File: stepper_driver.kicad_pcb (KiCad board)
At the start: 2 copper layers, 41.9 x 41.9 mm, 13 parts, among them T1 TERM_BLK_4_PIN_0.1_PITCH, T2 TERM_BLK_ANG_2_PIN_3.5MM_PITCH, T3 TERM_BLK_2_PIN_0.1_PITCH, T4 TERM_BLK_2_PIN_0.1_PITCH

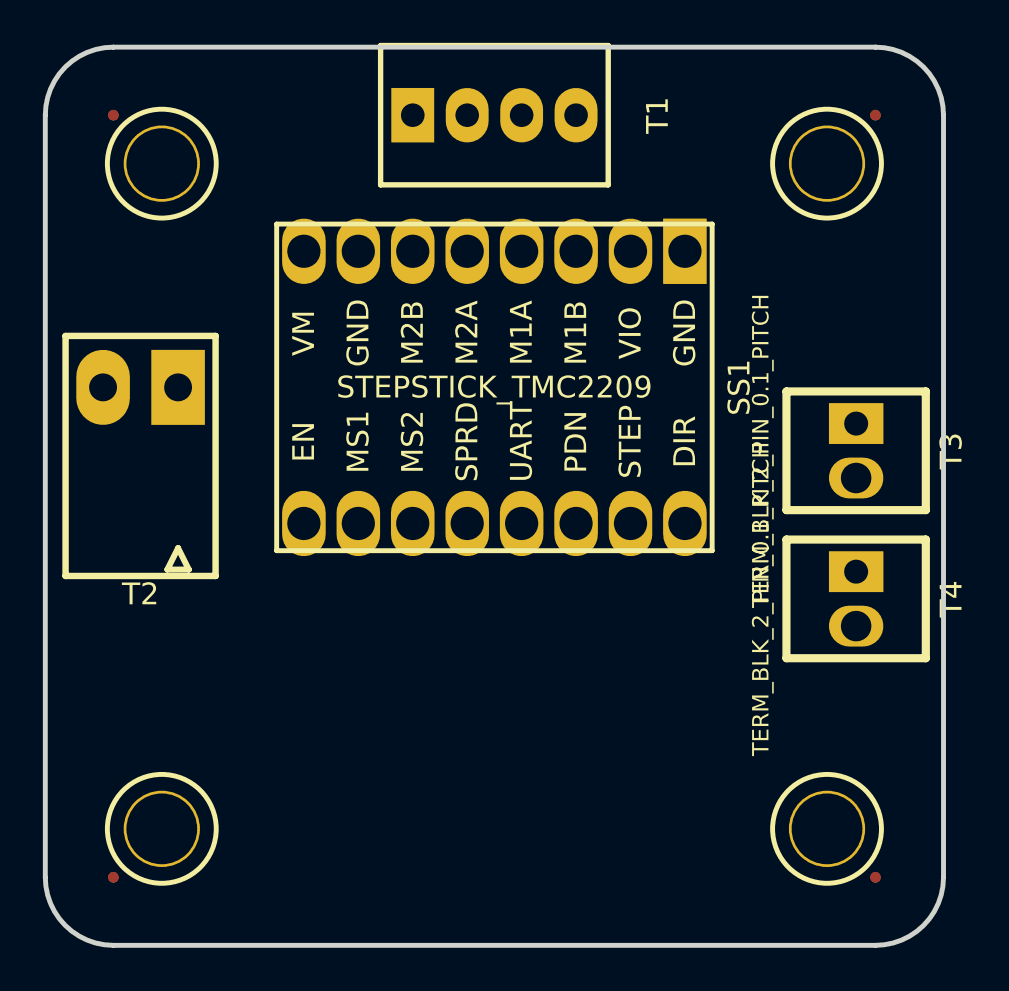
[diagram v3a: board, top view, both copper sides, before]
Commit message: Add power components
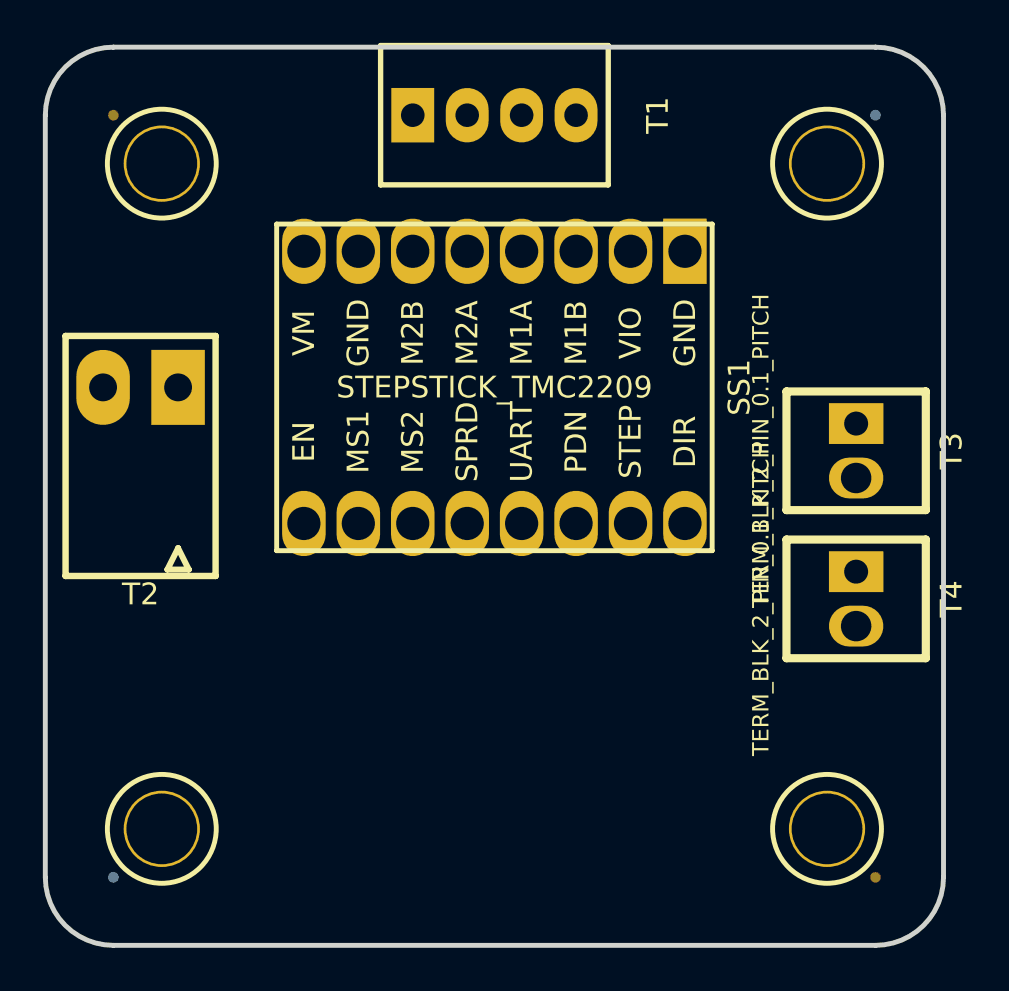
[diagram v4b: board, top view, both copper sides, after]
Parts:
- FID2, FID4: moved to B.Cu
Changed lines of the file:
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@@
       (effects (font (size 0.254 0.254) (thickness 0.0635)))
     )
+    (fp_circle (center 0 0) (end 0.5 0) (layer F.Fab) (width 0.1))
     (fp_circle (center 0 0) (end 0.75 0) (layer F.CrtYd) (width 0.05))
-    (fp_circle (center 0 0) (end 0.5 0) (layer F.Fab) (width 0.1))
     (fp_text user %R (at 0 0) (layer F.Fab)
       (effects (font (size 0.2 0.2) (thickness 0.04)))
@@
       (solder_mask_margin 0.25) (clearance 0.25))
   )
-  (module stepper_driver:FIDUCIAL (layer F.Cu)
+  (module stepper_driver:FIDUCIAL (layer B.Cu)
     (at 157.48 71.12)
     (descr "Circular Fiducial, 0.5mm bare copper top; 1mm keepout (Level C)")
     (tags marker)
     (attr virtual)
-    (fp_text reference FID2 (at 0 -1.016) (layer F.Fab)
-      (effects (font (size 0.254 0.254) (thickness 0.0635)))
-    )
-    (fp_text value FIDUCIAL (at 0 1.016) (layer F.Fab)
-      (effects (font (size 0.254 0.254) (thickness 0.0635)))
-    )
-    (fp_circle (center 0 0) (end 0.5 0) (layer F.Fab) (width 0.1))
-    (fp_circle (center 0 0) (end 0.75 0) (layer F.CrtYd) (width 0.05))
-    (fp_text user %R (at 0 0) (layer F.Fab)
-      (effects (font (size 0.2 0.2) (thickness 0.04)))
-    )
-    (pad ~ smd circle (at 0 0) (size 0.5 0.5) (layers F.Cu F.Mask)
+    (fp_text reference FID2 (at 0 1.016) (layer B.Fab)
+      (effects (font (size 0.254 0.254) (thickness 0.0635)) (justify mirror))
+    )
+    (fp_text value FIDUCIAL (at 0 -1.016) (layer B.Fab)
+      (effects (font (size 0.254 0.254) (thickness 0.0635)) (justify mirror))
+    )
+    (fp_circle (center 0 0) (end 0.75 0) (layer B.CrtYd) (width 0.05))
+    (fp_circle (center 0 0) (end 0.5 0) (layer B.Fab) (width 0.1))
+    (fp_text user %R (at 0 0) (layer B.Fab)
+      (effects (font (size 0.2 0.2) (thickness 0.04)) (justify mirror))
+    )
+    (pad ~ smd circle (at 0 0) (size 0.5 0.5) (layers B.Cu B.Mask)
       (solder_mask_margin 0.25) (clearance 0.25))
   )
@@
       (effects (font (size 0.254 0.254) (thickness 0.0635)))
     )
+    (fp_circle (center 0 0) (end 0.5 0) (layer F.Fab) (width 0.1))
     (fp_circle (center 0 0) (end 0.75 0) (layer F.CrtYd) (width 0.05))
-    (fp_circle (center 0 0) (end 0.5 0) (layer F.Fab) (width 0.1))
     (fp_text user %R (at 0 0) (layer F.Fab)
       (effects (font (size 0.2 0.2) (thickness 0.04)))
@@
       (solder_mask_margin 0.25) (clearance 0.25))
   )
-  (module stepper_driver:FIDUCIAL (layer F.Cu)
+  (module stepper_driver:FIDUCIAL (layer B.Cu)
     (at 121.92 106.68)
     (descr "Circular Fiducial, 0.5mm bare copper top; 1mm keepout (Level C)")
     (tags marker)
     (attr virtual)
-    (fp_text reference FID4 (at 0 -1.016) (layer F.Fab)
-      (effects (font (size 0.254 0.254) (thickness 0.0635)))
-    )
-    (fp_text value FIDUCIAL (at 0 1.016) (layer F.Fab)
-      (effects (font (size 0.254 0.254) (thickness 0.0635)))
-    )
-    (fp_circle (center 0 0) (end 0.5 0) (layer F.Fab) (width 0.1))
-    (fp_circle (center 0 0) (end 0.75 0) (layer F.CrtYd) (width 0.05))
-    (fp_text user %R (at 0 0) (layer F.Fab)
-      (effects (font (size 0.2 0.2) (thickness 0.04)))
-    )
-    (pad ~ smd circle (at 0 0) (size 0.5 0.5) (layers F.Cu F.Mask)
+    (fp_text reference FID4 (at 0 1.016) (layer B.Fab)
+      (effects (font (size 0.254 0.254) (thickness 0.0635)) (justify mirror))
+    )
+    (fp_text value FIDUCIAL (at 0 -1.016) (layer B.Fab)
+      (effects (font (size 0.254 0.254) (thickness 0.0635)) (justify mirror))
+    )
+    (fp_circle (center 0 0) (end 0.75 0) (layer B.CrtYd) (width 0.05))
+    (fp_circle (center 0 0) (end 0.5 0) (layer B.Fab) (width 0.1))
+    (fp_text user %R (at 0 0) (layer B.Fab)
+      (effects (font (size 0.2 0.2) (thickness 0.04)) (justify mirror))
+    )
+    (pad ~ smd circle (at 0 0) (size 0.5 0.5) (layers B.Cu B.Mask)
       (solder_mask_margin 0.25) (clearance 0.25))
   )
@@
       (effects (font (size 1.016 1.016) (thickness 0.254)))
     )
+    (fp_line (start 7.62 -10.16) (end -7.62 -10.16) (layer F.SilkS) (width 0.2286))
+    (fp_line (start 7.62 10.16) (end 7.62 -10.16) (layer F.SilkS) (width 0.2286))
+    (fp_line (start -7.62 10.16) (end 7.62 10.16) (layer F.SilkS) (width 0.2286))
     (fp_line (start -7.62 -10.16) (end -7.62 10.16) (layer F.SilkS) (width 0.2286))
-    (fp_line (start -7.62 10.16) (end 7.62 10.16) (layer F.SilkS) (width 0.2286))
-    (fp_line (start 7.62 10.16) (end 7.62 -10.16) (layer F.SilkS) (width 0.2286))
-    (fp_line (start 7.62 -10.16) (end -7.62 -10.16) (layer F.SilkS) (width 0.2286))
     (fp_text user DIR (at 2.54 -8.89 90) (layer F.SilkS)
       (effects (font (size 1.016 1.016) (thickness 0.254)))
@@
       (effects (font (size 0.762 0.762) (thickness 0.1905)))
     )
+    (fp_line (start -5.31 -3.25) (end 5.31 -3.25) (layer F.SilkS) (width 0.25))
+    (fp_line (start 5.31 -3.25) (end 5.31 3.25) (layer F.SilkS) (width 0.25))
+    (fp_line (start -5.31 3.25) (end 5.31 3.25) (layer F.SilkS) (width 0.25))
     (fp_line (start -5.31 -3.25) (end -5.31 3.25) (layer F.SilkS) (width 0.25))
-    (fp_line (start -5.31 3.25) (end 5.31 3.25) (layer F.SilkS) (width 0.25))
-    (fp_line (start 5.31 -3.25) (end 5.31 3.25) (layer F.SilkS) (width 0.25))
-    (fp_line (start -5.31 -3.25) (end 5.31 -3.25) (layer F.SilkS) (width 0.25))
     (pad 1 thru_hole rect (at -3.81 0) (size 2 2.54) (drill 1.1) (layers *.Cu *.Mask)
       (net 5 /B-))
@@
       (effects (font (size 0.508 0.508) (thickness 0.127)))
     )
+    (fp_line (start -3.5 -8.8) (end -3.5 2.4) (layer F.SilkS) (width 0.3))
+    (fp_line (start -3.5 2.4) (end 3.5 2.4) (layer F.SilkS) (width 0.3))
+    (fp_line (start 3.5 -8.8) (end 3.5 2.4) (layer F.SilkS) (width 0.3))
+    (fp_line (start -3.5 -8.8) (end 3.5 -8.8) (layer F.SilkS) (width 0.3))
+    (fp_line (start -2.25 -8.5) (end -1.25 -8.5) (layer F.SilkS) (width 0.2794))
+    (fp_line (start -1.25 -8.5) (end -1.75 -7.5) (layer F.SilkS) (width 0.2794))
     (fp_line (start -1.75 -7.5) (end -2.25 -8.5) (layer F.SilkS) (width 0.2794))
-    (fp_line (start -1.25 -8.5) (end -1.75 -7.5) (layer F.SilkS) (width 0.2794))
-    (fp_line (start -2.25 -8.5) (end -1.25 -8.5) (layer F.SilkS) (width 0.2794))
-    (fp_line (start -3.5 -8.8) (end 3.5 -8.8) (layer F.SilkS) (width 0.3))
-    (fp_line (start 3.5 -8.8) (end 3.5 2.4) (layer F.SilkS) (width 0.3))
-    (fp_line (start -3.5 2.4) (end 3.5 2.4) (layer F.SilkS) (width 0.3))
-    (fp_line (start -3.5 -8.8) (end -3.5 2.4) (layer F.SilkS) (width 0.3))
     (pad 1 thru_hole rect (at -1.75 0 180) (size 2.5 3.5) (drill 1.3) (layers *.Cu *.Mask))
     (pad 2 thru_hole oval (at 1.75 0 180) (size 2.5 3.5) (drill 1.3) (layers *.Cu *.Mask)
@@
     (at 156.578299 86.779101 270)
     (fp_text reference T3 (at 0 -4.445 90) (layer F.SilkS)
+      (effects (font (size 1.016 1.016) (thickness 0.254)))
+    )
+    (fp_text value TERM_BLK_2_PIN_0.1_PITCH (at 0 4.445 270) (layer F.SilkS)
+      (effects (font (size 0.762 0.762) (thickness 0.1905)))
+    )
+    (fp_line (start -2.7686 -3.2512) (end -2.7686 3.2512) (layer F.SilkS) (width 0.381))
+    (fp_line (start -2.7686 3.2512) (end 2.7686 3.2512) (layer F.SilkS) (width 0.381))
+    (fp_line (start 2.7686 -3.2512) (end 2.7686 3.2512) (layer F.SilkS) (width 0.381))
+    (fp_line (start -2.7686 -3.2512) (end 2.7686 -3.2512) (layer F.SilkS) (width 0.381))
+    (pad 1 thru_hole rect (at -1.27 0 270) (size 1.905 2.54) (drill 1.1176) (layers *.Cu *.Mask))
+    (pad 2 thru_hole oval (at 1.27 0 270) (size 1.905 2.54) (drill 1.4224) (layers *.Cu *.Mask))
+  )
+  (module stepper_driver:TERM_BLK_2_PIN_0.1_PITCH (layer F.Cu)
+    (at 156.578299 93.689101 270)
+    (fp_text reference T4 (at 0 -4.445 90) (layer F.SilkS)
       (effects (font (size 1.016 1.016) (thickness 0.254)))
     )
@@
     (fp_line (start -2.7686 3.2512) (end 2.7686 3.2512) (layer F.SilkS) (width 0.381))
     (fp_line (start -2.7686 -3.2512) (end -2.7686 3.2512) (layer F.SilkS) (width 0.381))
-    (pad 1 thru_hole rect (at -1.27 0 270) (size 1.905 2.54) (drill 1.1176) (layers *.Cu *.Mask))
-    (pad 2 thru_hole oval (at 1.27 0 270) (size 1.905 2.54) (drill 1.4224) (layers *.Cu *.Mask))
-  )
-  (module stepper_driver:TERM_BLK_2_PIN_0.1_PITCH (layer F.Cu)
-    (at 156.578299 93.689101 270)
-    (fp_text reference T4 (at 0 -4.445 90) (layer F.SilkS)
-      (effects (font (size 1.016 1.016) (thickness 0.254)))
-    )
-    (fp_text value TERM_BLK_2_PIN_0.1_PITCH (at 0 4.445 270) (layer F.SilkS)
-      (effects (font (size 0.762 0.762) (thickness 0.1905)))
-    )
-    (fp_line (start -2.7686 -3.2512) (end -2.7686 3.2512) (layer F.SilkS) (width 0.381))
-    (fp_line (start -2.7686 3.2512) (end 2.7686 3.2512) (layer F.SilkS) (width 0.381))
-    (fp_line (start 2.7686 -3.2512) (end 2.7686 3.2512) (layer F.SilkS) (width 0.381))
-    (fp_line (start -2.7686 -3.2512) (end 2.7686 -3.2512) (layer F.SilkS) (width 0.381))
     (pad 2 thru_hole oval (at 1.27 0 270) (size 1.905 2.54) (drill 1.4224) (layers *.Cu *.Mask))
     (pad 1 thru_hole rect (at -1.27 0 270) (size 1.905 2.54) (drill 1.1176) (layers *.Cu *.Mask))

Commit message: Add latched header
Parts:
- added C1: 100uF_POL, stepper_driver:CP_Elec_6.3x7.7_WURTH, B.Cu at (134.6, 82.5)
- added C2: 1uF, stepper_driver:SM0402, F.Cu at (163.4, 121.4)
- added C3: 1uF, stepper_driver:SM0402, F.Cu at (141.7, 132.4)
- added C4: 0.1uF, stepper_driver:SM0402, F.Cu at (156.8, 124.2)
- added C5: 0.1uF, stepper_driver:SM0402, F.Cu at (143.6, 132.4)
- added D1: DIODE_SCHOTTKY_45V_10A, stepper_driver:CFP15, B.Cu at (127.0, 87.6)
- added D2: DIODE_TVS_ZENER_28V, stepper_driver:D_SMB_LITTELFUSE, B.Cu at (121.9, 87.6)
- added P1: HEADER_02X05_LATCH, stepper_driver:HEADER_02x05_LATCH, F.Cu at (139.7, 96.5)
- added R1: 100, stepper_driver:SM0402, F.Cu at (148.4, 129.8)
- added R2: 100, stepper_driver:SM0402, F.Cu at (145.6, 132.4)
- added REG1: CONV_DC_DC_3.3V_100MA, stepper_driver:SOT-23-3, F.Cu at (138.8, 133.1)
- added U1: SN65LVDM050QDRQ1, stepper_driver:SOIC_16_0.154IN, B.Cu at (139.7, 104.1)
- moved T3 6.78 mm to (156.2, 80.0)
- moved T4 6.06 mm to (156.6, 87.6)
- moved T2 2.54 mm to (123.2, 81.3)
- moved SS1 1.27 mm to (139.7, 82.5)
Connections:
- SS1 pad 10: (no net) -> /STEP
- SS1 pad 12: (no net) -> /UART
- SS1 pad 2: (no net) -> /VDD
- SS1 pad 8: (no net) -> /VCC
- SS1 pad 9: (no net) -> /DIR
- T2 pad 1: (no net) -> /VAA
- T3 pad 1: (no net) -> /GND
- T4 pad 1: (no net) -> /GND

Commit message: Prepare for routing
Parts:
- added U2: MAX6817, stepper_driver:MAX6817, B.Cu at (153.0, 84.5)
- C2, C3, C4, C5, R1, R2, REG1: moved to B.Cu
- T1: value TERM_BLK_4_PIN_0.1_PITCH -> TERM_BLK_4_PIN
- T3, T4: value TERM_BLK_2_PIN_0.1_PITCH -> TERM_BLK_2_PIN
- moved C5 52.0 mm to (153.0, 81.3), turned to 270 degrees
- moved REG1 49.1 mm to (144.8, 84.5)
- moved C3 48.3 mm to (148.0, 84.5), turned to 180 degrees
- moved C2 42.9 mm to (141.6, 84.5), turned to 180 degrees
- moved R2 31.6 mm to (142.2, 101.0), turned to 270 degrees
- moved R1 31.4 mm to (135.9, 101.0), turned to 90 degrees
- moved C4 30.1 mm to (133.3, 105.4)
- moved C1 1.91 mm to (134.6, 84.5)
- moved SS1 1.91 mm to (139.7, 84.5)
- moved U1 1.27 mm to (139.7, 105.4), turned to 270 degrees
- moved T2 1.14 mm to (124.3, 81.3)
- moved T3 0.90 mm to (156.8, 80.6)
- moved T4 0.69 mm to (156.8, 88.3)
- moved P1 0.64 mm to (139.7, 97.2), turned to 180 degrees
- moved T1 0.38 mm to (139.7, 71.5)
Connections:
- T3 pad 2: (no net) -> /REF
- T4 pad 2: (no net) -> /REFR
- U1 pad 15: (no net) -> /REF_D
- U1 pad 9: (no net) -> /REFR_D
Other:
- net class GROUND added: clearance 0.1016, trace_width 0.4064, via_dia 0.889, via_drill 0.635
- board text added: "5-24VDC"
- board text added: "A+"
- board text added: "A-"
- board text added: "B+"
- board text added: "B-"
- board text added: "GND"
- board text added: "REF"
- board text added: "REFR"

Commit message: Initial routing
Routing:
- net /GND: track 0.00 -> 141.5 mm, vias 0 -> 1
- net /VDD: track 0.00 -> 79.0 mm, vias 0 -> 2
- net /REF_D: track 0.00 -> 39.5 mm
- net /VCC: track 0.00 -> 32.0 mm
- net /STEP: track 0.00 -> 29.4 mm
- net /REFR_D: track 0.00 -> 26.6 mm
- net /DIR: track 0.00 -> 17.7 mm, vias 0 -> 1
- net /REF_A: track 0.00 -> 17.5 mm
- net /REFR_B: track 0.00 -> 15.2 mm, vias 0 -> 1
- net /REF_B: track 0.00 -> 13.7 mm, vias 0 -> 1
- net /REFR_A: track 0.00 -> 11.1 mm
- net /DIR_B: track 0.00 -> 10.6 mm
- net /STEP_B: track 0.00 -> 8.83 mm
- net /UART: track 0.00 -> 8.29 mm
- net /DIR_A: track 0.00 -> 7.87 mm
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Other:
- net class GROUND: trace_width 0.4064 -> 0.8128; via_dia 0.889 -> 1.0668
- net class POWER: trace_width 0.2032 -> 0.8128; via_dia 0.6096 -> 1.0668; via_drill 0.4064 -> 0.635
- net class SENSE: via_drill 0.6096 -> 0.635
- net class SIGNAL: trace_width 0.2032 -> 0.4064; via_dia 0.6096 -> 0.889; via_drill 0.4064 -> 0.635
- net class THICKPOWER: trace_width 0.6096 -> 1.524; via_dia 0.9144 -> 1.524; via_drill 0.4064 -> 0.635
- net class THICKSIGNAL: via_drill 0.4064 -> 0.635
- board text added: "stepper_driver NEMA 17 Janelia Research Campus 11/2021 ver 1.0"

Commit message: Finish v1.0 layout
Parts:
- MH1, MH2, MH3, MH4: value MOUNTING_HOLE_4-40 -> VAL**
- U2: value MAX6817 -> VAL**
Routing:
- added copper zone on B.Cu, net /GND
- added copper zone on F.Cu, net /GND
